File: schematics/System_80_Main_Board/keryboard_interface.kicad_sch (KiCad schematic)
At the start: 8 parts, among them J4 Keyboard, U2 74LS05, U3 74LS05, U7 74LS368, U8 74LS368

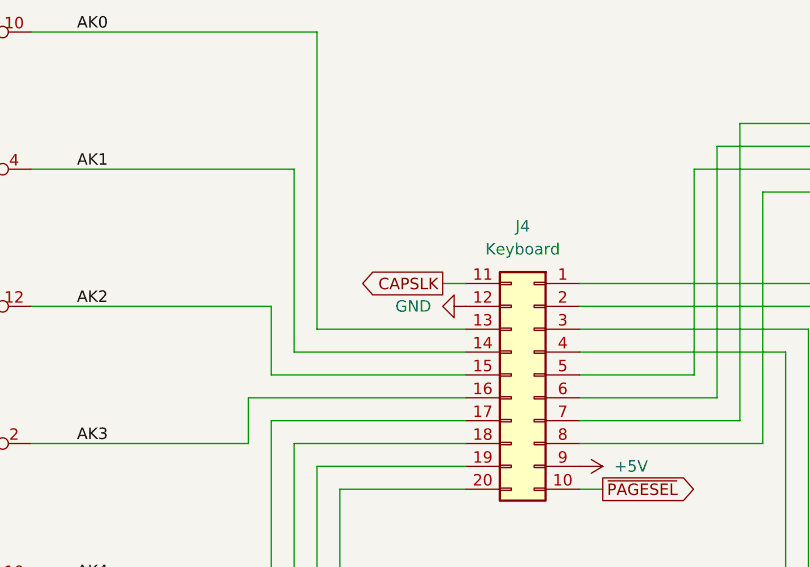
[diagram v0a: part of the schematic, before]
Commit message: Schematic for the System 80 video/cassette board
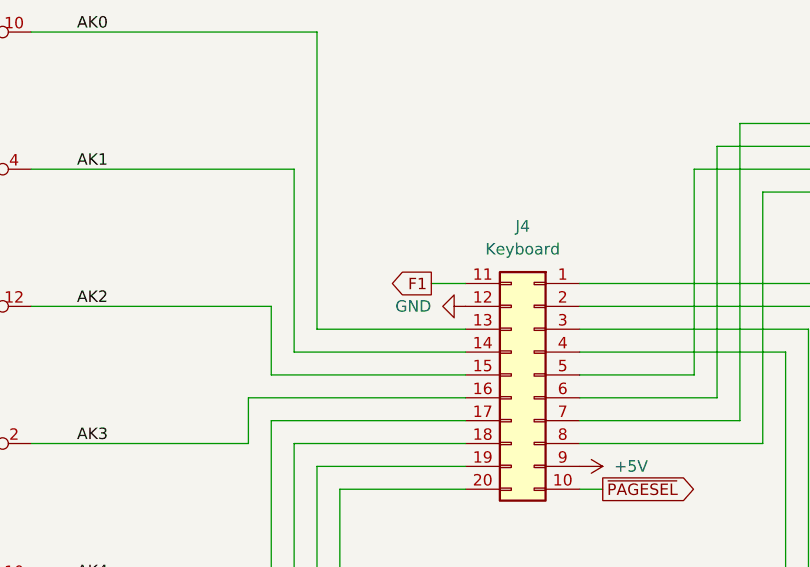
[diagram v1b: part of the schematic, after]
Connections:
- net CAPSLK renamed F1
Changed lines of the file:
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@@
 	(wire
 		(pts
-			(xy 123.19 92.71) (xy 125.73 92.71)
+			(xy 121.92 92.71) (xy 125.73 92.71)
 		)
 		(stroke
@@
 		)
 	)
-	(global_label "CAPSLK"
+	(global_label "F1"
 		(shape output)
-		(at 123.19 92.71 180)
+		(at 121.92 92.71 180)
 		(fields_autoplaced yes)
 		(effects
@@
 		)
 		(property "Intersheetrefs" "${INTERSHEET_REFS}"
-			(at 113.0686 92.71 0)
+			(at 116.6367 92.71 0)
 			(effects
 				(font
